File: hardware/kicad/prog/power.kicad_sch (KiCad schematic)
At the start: 17 parts, among them J1 AES PROG, J2 Câble PROG-CHA, U1 AMS1117-3.3, U2 AP2112K-1.2

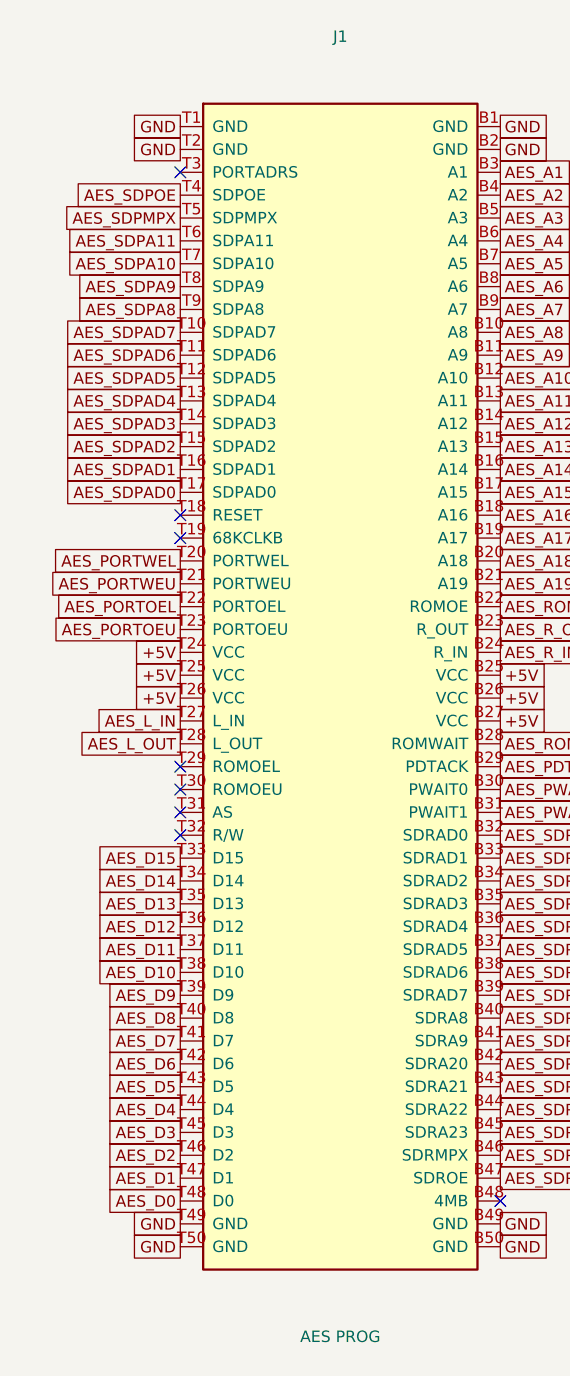
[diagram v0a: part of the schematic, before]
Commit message: Connecteur AES : numérotation officielle, empreinte et contours des cartes
Recoupement avec les cartes AES de jwestfall69 (neogeo-diag-aes-prog et
neogeo-diag-aes-cha, fabriquées et testées, domaine public) :
- la face « dessus » (contacts A, côté composants) était numérotée à
  l'envers : position n -> 51 - n. A1 et B1 sont à droite vus côté
  composants, l'un derrière l'autre (sérigraphie A1 des cartes NEO-AEG) ;
  face B inchangée. Les 200 contacts concordent désormais.
- empreinte : contacts 1,5 x 10 mm, centre à 7,1 mm du bord, T1 à droite.
- hardware/gen/outline.py : contours PROG (174 x 115 mm) et CHA
  (173 x 115 mm), languette 129,2 x 19 mm, encoches, trous de 10 mm et J1
  placé ; identiques aux cartes de référence à 0,01 mm près, recoupés
  sur la photo NEO-AEG PROG-EP du wiki.
Schémas, PDF, .pcf et documentation régénérés ; netlists identiques.

Co-Authored-By: Claude Opus 5.5 <noreply@anthropic.com>
Claude-Session: https://claude.ai/code/session_01WKfXP1YJ8otGxZ5dsY6Agh
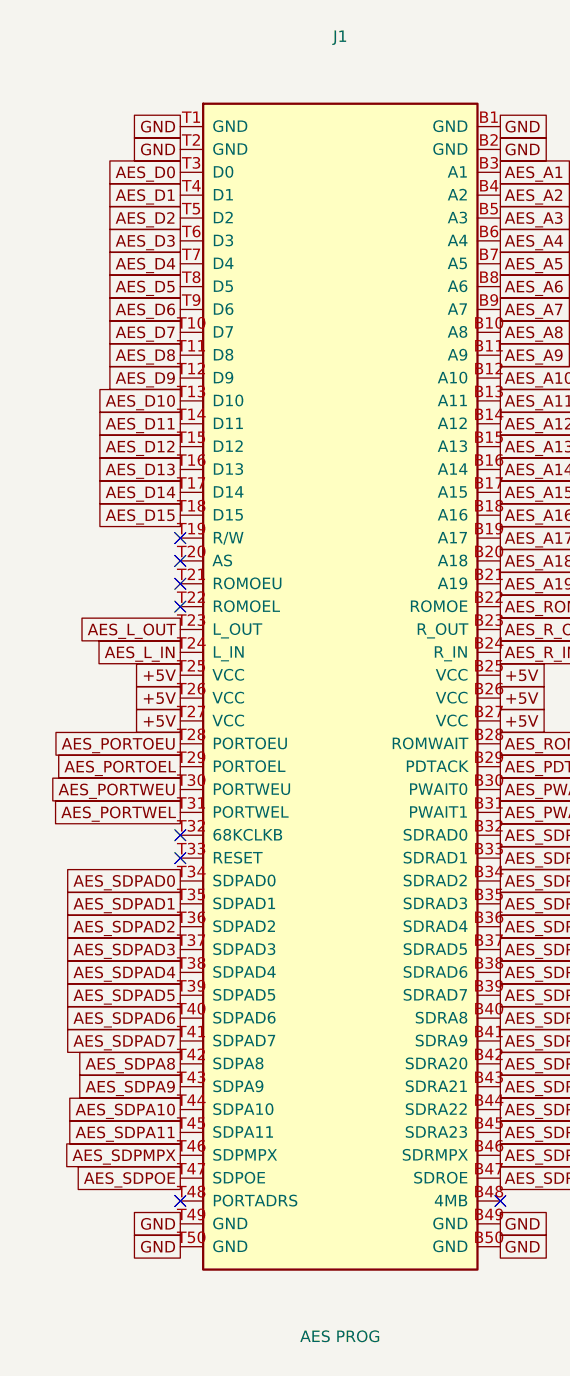
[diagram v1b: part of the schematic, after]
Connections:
- net +5V: now also J1.T27 (VCC); no longer J1.T24 (VCC)
- net AES_D0: now also J1.T3 (D0); no longer J1.T48 (D0)
- net AES_D1: now also J1.T4 (D1); no longer J1.T47 (D1)
- net AES_D10: now also J1.T13 (D10); no longer J1.T38 (D10)
- net AES_D11: now also J1.T14 (D11); no longer J1.T37 (D11)
- net AES_D12: now also J1.T15 (D12); no longer J1.T36 (D12)
- net AES_D13: now also J1.T16 (D13); no longer J1.T35 (D13)
- net AES_D14: now also J1.T17 (D14); no longer J1.T34 (D14)
- net AES_D15: now also J1.T18 (D15); no longer J1.T33 (D15)
- net AES_D2: now also J1.T5 (D2); no longer J1.T46 (D2)
- net AES_D3: now also J1.T6 (D3); no longer J1.T45 (D3)
- net AES_D4: now also J1.T7 (D4); no longer J1.T44 (D4)
- net AES_D5: now also J1.T8 (D5); no longer J1.T43 (D5)
- net AES_D6: now also J1.T9 (D6); no longer J1.T42 (D6)
- net AES_D7: now also J1.T10 (D7); no longer J1.T41 (D7)
- net AES_D8: now also J1.T11 (D8); no longer J1.T40 (D8)
- net AES_D9: now also J1.T12 (D9); no longer J1.T39 (D9)
- net AES_L_IN: now also J1.T24 (L_IN); no longer J1.T27 (L_IN)
- net AES_L_OUT: now also J1.T23 (L_OUT); no longer J1.T28 (L_OUT)
- net AES_PORTOEL: now also J1.T29 (PORTOEL); no longer J1.T22 (PORTOEL)
- net AES_PORTOEU: now also J1.T28 (PORTOEU); no longer J1.T23 (PORTOEU)
- net AES_PORTWEL: now also J1.T31 (PORTWEL); no longer J1.T20 (PORTWEL)
- net AES_PORTWEU: now also J1.T30 (PORTWEU); no longer J1.T21 (PORTWEU)
- net AES_SDPA10: now also J1.T44 (SDPA10); no longer J1.T7 (SDPA10)
- net AES_SDPA11: now also J1.T45 (SDPA11); no longer J1.T6 (SDPA11)
- net AES_SDPA8: now also J1.T42 (SDPA8); no longer J1.T9 (SDPA8)
- net AES_SDPA9: now also J1.T43 (SDPA9); no longer J1.T8 (SDPA9)
- net AES_SDPAD0: now also J1.T34 (SDPAD0); no longer J1.T17 (SDPAD0)
- net AES_SDPAD1: now also J1.T35 (SDPAD1); no longer J1.T16 (SDPAD1)
- net AES_SDPAD2: now also J1.T36 (SDPAD2); no longer J1.T15 (SDPAD2)
- net AES_SDPAD3: now also J1.T37 (SDPAD3); no longer J1.T14 (SDPAD3)
- net AES_SDPAD4: now also J1.T38 (SDPAD4); no longer J1.T13 (SDPAD4)
- net AES_SDPAD5: now also J1.T39 (SDPAD5); no longer J1.T12 (SDPAD5)
- net AES_SDPAD6: now also J1.T40 (SDPAD6); no longer J1.T11 (SDPAD6)
- net AES_SDPAD7: now also J1.T41 (SDPAD7); no longer J1.T10 (SDPAD7)
- net AES_SDPMPX: now also J1.T46 (SDPMPX); no longer J1.T5 (SDPMPX)
- net AES_SDPOE: now also J1.T47 (SDPOE); no longer J1.T4 (SDPOE)

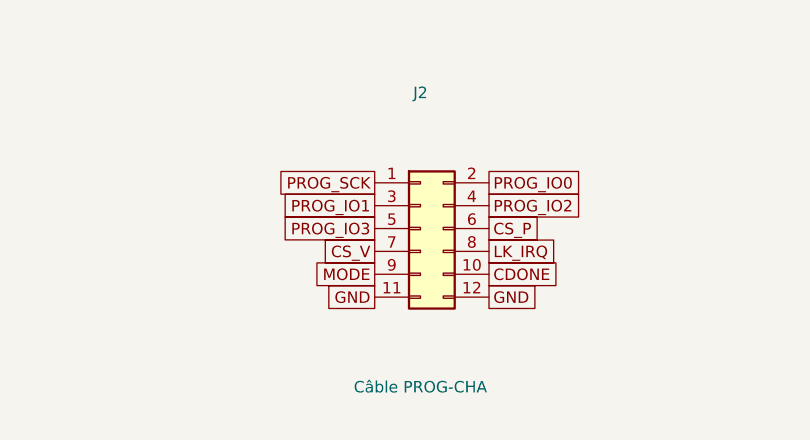
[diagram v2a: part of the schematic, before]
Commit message: FPGA configurés par le RP2350 depuis la carte SD (plus de flash)
- Matériel : flash SPI retirées (4 W25Q32, 12 résistances, 4
  condensateurs). Le bus de liaison arrive sur les broches de
  configuration des iCE40 (LK_SCK -> 70 SCK, LK_IO[0] -> 68 SDI,
  LK_CS_N -> 71 SS), qui redeviennent ces entrées après le démarrage.
  CRESET_N commun aux 4 FPGA, tiré à la masse, piloté par le RP2350
  (GP28) ; câble PROG-CHA en 2 x 7 (CRESET_N + masse). Connecteur 2 x 3
  de secours par FPGA (iceprog -S).
- Firmware : fpga_boot.c (reset commun en mode SPI esclave, envoi des
  SDAES/fpga_*.bin l'un après l'autre, contrôle de CDONE) ; testé sur
  PC (bitstreams reçus à l'identique, FPGA laissés en reset si un
  fichier manque).
- make -C hdl sd : fichiers à copier sur la carte SD.
- PCB : table de placement et références des FPGA mises à jour,
  broches réoptimisées.
Placement-routage des FPGA avec les nouvelles broches : en cours.

Co-Authored-By: Claude Opus 5.5 <noreply@anthropic.com>
Claude-Session: https://claude.ai/code/session_01WKfXP1YJ8otGxZ5dsY6Agh
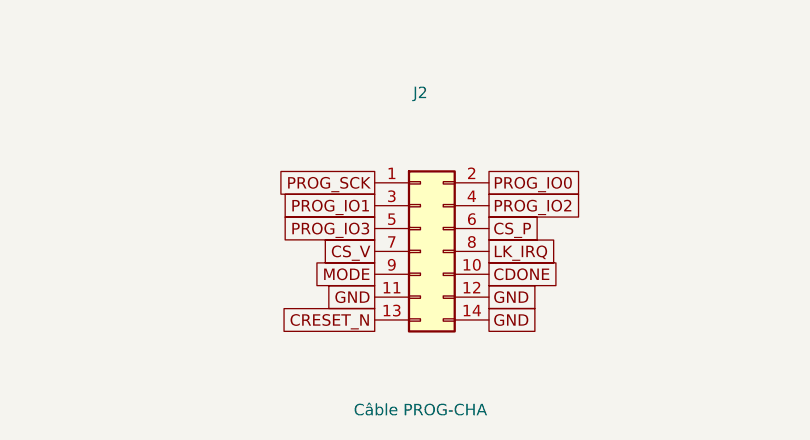
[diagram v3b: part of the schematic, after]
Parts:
- removed J2: Câble PROG-CHA, Connector_PinHeader_2.54mm:PinHeader_2x06_P2.54mm_Vertical, symbol Connector_Generic:Conn_02x06_Odd_Even
- added J2: Câble PROG-CHA, Connector_PinHeader_2.54mm:PinHeader_2x07_P2.54mm_Vertical, symbol Connector_Generic:Conn_02x07_Odd_Even
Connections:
- net CDONE: now also J2.10 (Pin_10)
- net CS_P: now also J2.6 (Pin_6)
- net CS_V: now also J2.7 (Pin_7)
- net GND: now also J2.11 (Pin_11), J2.12 (Pin_12), J2.14 (Pin_14)
- net LK_IRQ: now also J2.8 (Pin_8)
- net MODE: now also J2.9 (Pin_9)
- net PROG_IO0: now also J2.2 (Pin_2)
- net PROG_IO1: now also J2.3 (Pin_3)
- net PROG_IO2: now also J2.4 (Pin_4)
- net PROG_IO3: now also J2.5 (Pin_5)
- net PROG_SCK: now also J2.1 (Pin_1)
- new net CRESET_N: J2.13 (Pin_13)
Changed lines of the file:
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@@
     (instances
       (project "prog"
-        (path "/a2c04eda-906b-4407-9534-e4dc8a098a56/a14df387-67dc-45ee-b7ad-5dc8e6fa0ac0"
+        (path "/773ca91f-e149-4bba-abf7-6085382b056a/a6a92b0d-f06c-49b0-859a-21fba0d9e0d0"
           (reference "J1")
           (unit 1)))))
@@
     (instances
       (project "prog"
-        (path "/a2c04eda-906b-4407-9534-e4dc8a098a56/a14df387-67dc-45ee-b7ad-5dc8e6fa0ac0"
+        (path "/773ca91f-e149-4bba-abf7-6085382b056a/a6a92b0d-f06c-49b0-859a-21fba0d9e0d0"
           (reference "R1")
           (unit 1)))))
@@
     (instances
       (project "prog"
-        (path "/a2c04eda-906b-4407-9534-e4dc8a098a56/a14df387-67dc-45ee-b7ad-5dc8e6fa0ac0"
+        (path "/773ca91f-e149-4bba-abf7-6085382b056a/a6a92b0d-f06c-49b0-859a-21fba0d9e0d0"
           (reference "R2")
           (unit 1)))))
@@
     (instances
       (project "prog"
-        (path "/a2c04eda-906b-4407-9534-e4dc8a098a56/a14df387-67dc-45ee-b7ad-5dc8e6fa0ac0"
+        (path "/773ca91f-e149-4bba-abf7-6085382b056a/a6a92b0d-f06c-49b0-859a-21fba0d9e0d0"
           (reference "C1")
           (unit 1)))))
@@
     (instances
       (project "prog"
-        (path "/a2c04eda-906b-4407-9534-e4dc8a098a56/a14df387-67dc-45ee-b7ad-5dc8e6fa0ac0"
+        (path "/773ca91f-e149-4bba-abf7-6085382b056a/a6a92b0d-f06c-49b0-859a-21fba0d9e0d0"
           (reference "C2")
           (unit 1)))))
@@
     (instances
       (project "prog"
-        (path "/a2c04eda-906b-4407-9534-e4dc8a098a56/a14df387-67dc-45ee-b7ad-5dc8e6fa0ac0"
+        (path "/773ca91f-e149-4bba-abf7-6085382b056a/a6a92b0d-f06c-49b0-859a-21fba0d9e0d0"
           (reference "U1")
           (unit 1)))))
@@
     (instances
       (project "prog"
-        (path "/a2c04eda-906b-4407-9534-e4dc8a098a56/a14df387-67dc-45ee-b7ad-5dc8e6fa0ac0"
+        (path "/773ca91f-e149-4bba-abf7-6085382b056a/a6a92b0d-f06c-49b0-859a-21fba0d9e0d0"
           (reference "C3")
           (unit 1)))))
@@
     (instances
       (project "prog"
-        (path "/a2c04eda-906b-4407-9534-e4dc8a098a56/a14df387-67dc-45ee-b7ad-5dc8e6fa0ac0"
+        (path "/773ca91f-e149-4bba-abf7-6085382b056a/a6a92b0d-f06c-49b0-859a-21fba0d9e0d0"
           (reference "C4")
           (unit 1)))))
@@
     (instances
       (project "prog"
-        (path "/a2c04eda-906b-4407-9534-e4dc8a098a56/a14df387-67dc-45ee-b7ad-5dc8e6fa0ac0"
+        (path "/773ca91f-e149-4bba-abf7-6085382b056a/a6a92b0d-f06c-49b0-859a-21fba0d9e0d0"
           (reference "U2")
           (unit 1)))))
@@
     (instances
       (project "prog"
-        (path "/a2c04eda-906b-4407-9534-e4dc8a098a56/a14df387-67dc-45ee-b7ad-5dc8e6fa0ac0"
+        (path "/773ca91f-e149-4bba-abf7-6085382b056a/a6a92b0d-f06c-49b0-859a-21fba0d9e0d0"
           (reference "C5")
           (unit 1)))))
@@
     (instances
       (project "prog"
-        (path "/a2c04eda-906b-4407-9534-e4dc8a098a56/a14df387-67dc-45ee-b7ad-5dc8e6fa0ac0"
+        (path "/773ca91f-e149-4bba-abf7-6085382b056a/a6a92b0d-f06c-49b0-859a-21fba0d9e0d0"
           (reference "C6")
           (unit 1)))))
@@
     (instances
       (project "prog"
-        (path "/a2c04eda-906b-4407-9534-e4dc8a098a56/a14df387-67dc-45ee-b7ad-5dc8e6fa0ac0"
+        (path "/773ca91f-e149-4bba-abf7-6085382b056a/a6a92b0d-f06c-49b0-859a-21fba0d9e0d0"
           (reference "R3")
           (unit 1)))))
@@
     (instances
       (project "prog"
-        (path "/a2c04eda-906b-4407-9534-e4dc8a098a56/a14df387-67dc-45ee-b7ad-5dc8e6fa0ac0"
+        (path "/773ca91f-e149-4bba-abf7-6085382b056a/a6a92b0d-f06c-49b0-859a-21fba0d9e0d0"
           (reference "R4")
           (unit 1)))))
@@
     (instances
       (project "prog"
-        (path "/a2c04eda-906b-4407-9534-e4dc8a098a56/a14df387-67dc-45ee-b7ad-5dc8e6fa0ac0"
+        (path "/773ca91f-e149-4bba-abf7-6085382b056a/a6a92b0d-f06c-49b0-859a-21fba0d9e0d0"
           (reference "R5")
           (unit 1)))))
@@
     (instances
       (project "prog"
-        (path "/a2c04eda-906b-4407-9534-e4dc8a098a56/a14df387-67dc-45ee-b7ad-5dc8e6fa0ac0"
+        (path "/773ca91f-e149-4bba-abf7-6085382b056a/a6a92b0d-f06c-49b0-859a-21fba0d9e0d0"
           (reference "R6")
           (unit 1)))))
@@
     (instances
       (project "prog"
-        (path "/a2c04eda-906b-4407-9534-e4dc8a098a56/a14df387-67dc-45ee-b7ad-5dc8e6fa0ac0"
+        (path "/773ca91f-e149-4bba-abf7-6085382b056a/a6a92b0d-f06c-49b0-859a-21fba0d9e0d0"
           (reference "R7")
           (unit 1)))))
@@
           (size 1.27 1.27)) hide)))
   (symbol
-    (lib_id "Connector_Generic:Conn_02x06_Odd_Even")
-    (at 279.4 193.04 0)
+    (lib_id "Connector_Generic:Conn_02x07_Odd_Even")
+    (at 279.4 195.58 0)
     (unit 1)
     (in_bom yes)
@@
           (size 1.27 1.27))))
     (property "Value" "Câble PROG-CHA"
-      (at 279.4 210.66 0)
-      (effects
-        (font
-          (size 1.27 1.27))))
-    (property "Footprint" "Connector_PinHeader_2.54mm:PinHeader_2x06_P2.54mm_Vertical"
-      (at 279.4 193.04 0)
+      (at 279.4 213.2 0)
+      (effects
+        (font
+          (size 1.27 1.27))))
+    (property "Footprint" "Connector_PinHeader_2.54mm:PinHeader_2x07_P2.54mm_Vertical"
+      (at 279.4 195.58 0)
       (effects
         (font
           (size 1.27 1.27)) hide))
     (property "Datasheet" "~"
-      (at 279.4 193.04 0)
+      (at 279.4 195.58 0)
       (effects
         (font
@@
 )
     (pin "12"
+)
+    (pin "13"
+)
+    (pin "14"
 )
     (pin "2"
@@
     (instances
       (project "prog"
-        (path "/a2c04eda-906b-4407-9534-e4dc8a098a56/a14df387-67dc-45ee-b7ad-5dc8e6fa0ac0"
+        (path "/773ca91f-e149-4bba-abf7-6085382b056a/a6a92b0d-f06c-49b0-859a-21fba0d9e0d0"
           (reference "J2")
           (unit 1)))))
@@
       (effects
         (font
+          (size 1.27 1.27)) hide)))
+  (global_label "CRESET_N"
+    (shape passive)
+    (at 274.32 203.2 180)
+    (fields_autoplaced)
+    (effects
+      (font
+        (size 1.27 1.27))
+      (justify right))
+    (property "Intersheetrefs" "${INTERSHEET_REFS}"
+      (at 274.32 203.2 0)
+      (effects
+        (font
+          (size 1.27 1.27)) hide)))
+  (global_label "GND"
+    (shape passive)
+    (at 287.02 203.2 0)
+    (fields_autoplaced)
+    (effects
+      (font
+        (size 1.27 1.27))
+      (justify left))
+    (property "Intersheetrefs" "${INTERSHEET_REFS}"
+      (at 287.02 203.2 0)
+      (effects
+        (font
